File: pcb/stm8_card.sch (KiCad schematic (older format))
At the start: 22 parts, among them J1 DEBUG HEADER, SW1 TL59AF100Q, SW2 TL59AF100Q, SW3 TL59AF100Q, SW4 TL3302AF260QG, U1 ER-OLED0.91-7, U2 STM8S103F3

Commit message: pcb updated bat footprint in schematic not just board
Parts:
- BT1: footprint Battery:BatteryHolder_Keystone_103_1x20mm -> stm8_card:BatteryHolder_Keystone_103_1x20mm_Corrected
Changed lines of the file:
@@
 F 0 "BT1" H 1550 4500 50  0000 L CNN
 F 1 "103" H 1418 4405 50  0001 L CNN
-F 2 "Battery:BatteryHolder_Keystone_103_1x20mm" V 1300 4460 50  0001 C CNN
+F 2 "stm8_card:BatteryHolder_Keystone_103_1x20mm_Corrected" V 1300 4460 50  0001 C CNN
 F 3 "~" V 1300 4460 50  0001 C CNN
 F 4 "36-103-ND" H 1650 4400 50  0000 C CNN "digikey"

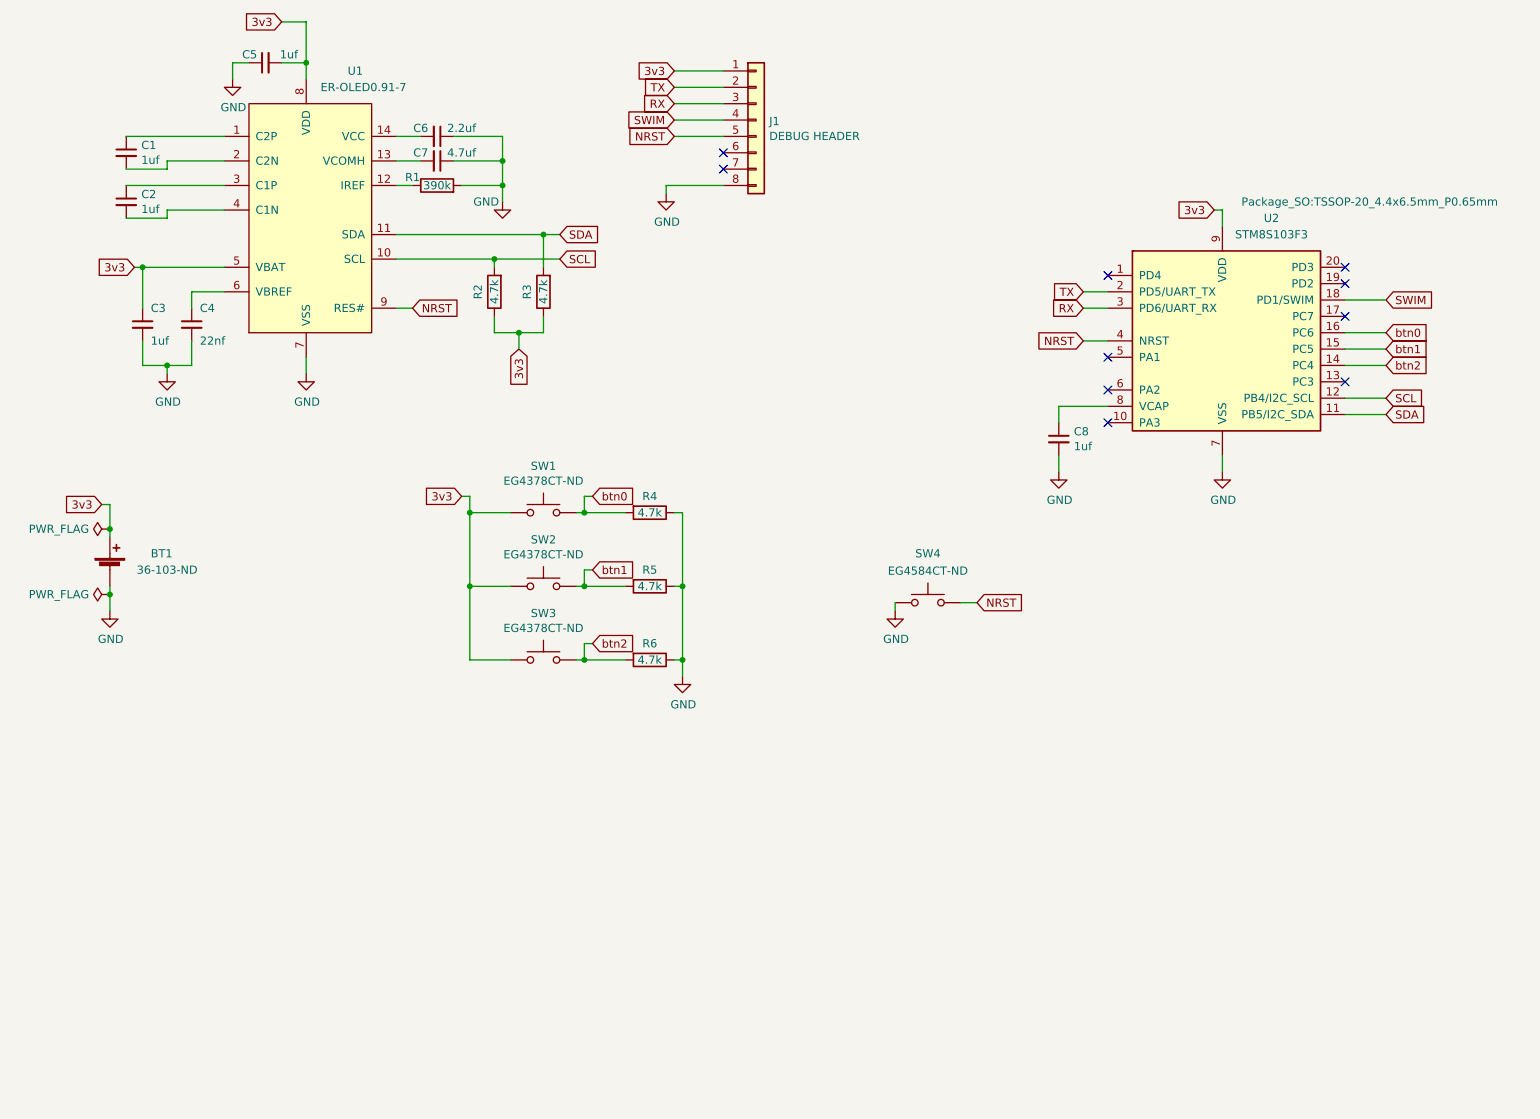
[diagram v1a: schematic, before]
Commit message: pcb improved pcb + added led, res, and mcu cap
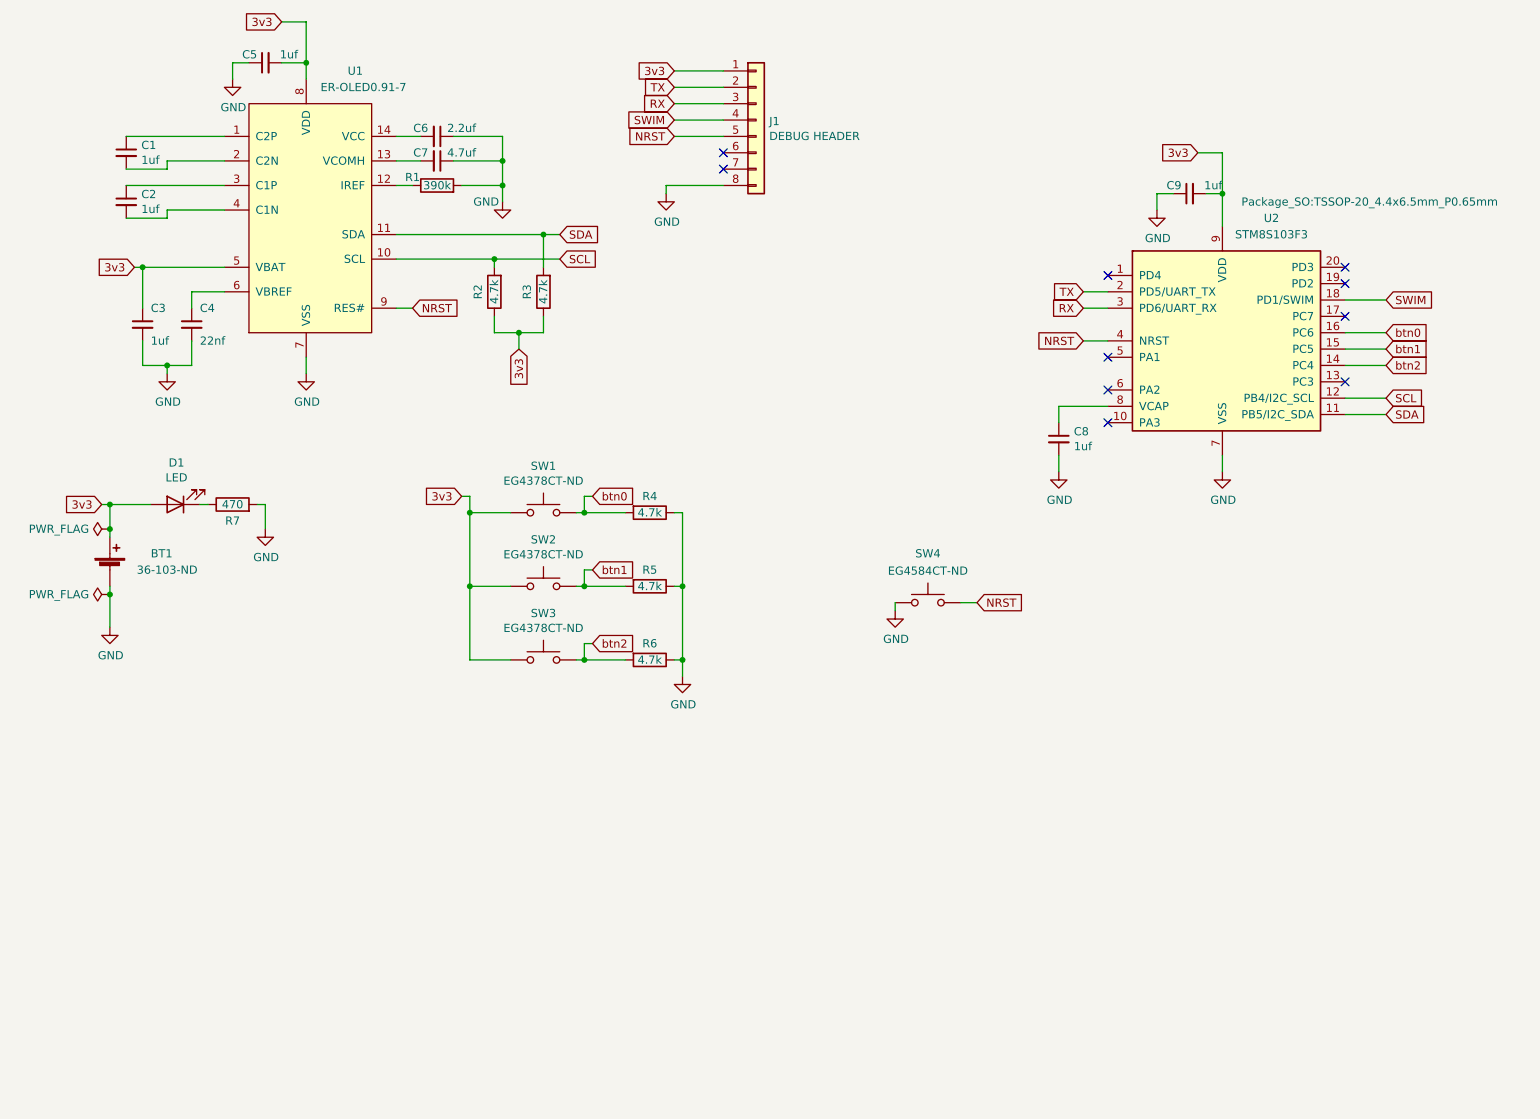
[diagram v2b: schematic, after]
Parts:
- added C9: 1uf, Capacitor_SMD:C_0805_2012Metric_Pad1.18x1.45mm_HandSolder, symbol Device:C_Small
- added D1: LED, stm8_card:LED_0805_2012Metric_Pad1.15x1.40mm_HandSolder, symbol Device:LED
- added R7: 470, Resistor_SMD:R_0805_2012Metric_Pad1.20x1.40mm_HandSolder, symbol Device:R
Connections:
- net 3v3: now also C9.2, D1.2 (A)
- net GND: now also C9.1, R7.2
- new net: D1.1 (K), R7.1
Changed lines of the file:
@@
 Wire Wire Line
 	8850 3450 9100 3450
-Text GLabel 8050 2200 0    50   Input ~ 0
+Text GLabel 7950 1850 0    50   Input ~ 0
 3v3
-Wire Wire Line
-	8050 2200 8100 2200
-Wire Wire Line
-	8100 2200 8100 2300
 Wire Wire Line
 	3150 2800 3050 2800
@@
 L power:GND #PWR01
 U 1 1 60827C7E
-P 1300 4650
-F 0 "#PWR01" H 1300 4400 50  0001 C CNN
-F 1 "GND" H 1305 4477 50  0000 C CNN
-F 2 "" H 1300 4650 50  0001 C CNN
-F 3 "" H 1300 4650 50  0001 C CNN
-	1    1300 4650
+P 2250 4150
+F 0 "#PWR01" H 2250 3900 50  0001 C CNN
+F 1 "GND" H 2255 3977 50  0000 C CNN
+F 2 "" H 2250 4150 50  0001 C CNN
+F 3 "" H 2250 4150 50  0001 C CNN
+	1    2250 4150
 	1    0    0    -1
 $EndComp
@@
 Connection ~ 1300 4550
 Wire Wire Line
-	1300 4550 1300 4650
-Wire Wire Line
 	2050 1300 2050 1400
 Wire Wire Line
@@
 Wire Wire Line
 	2350 1050 2500 1050
+$Comp
+L Device:C_Small C9
+U 1 1 6086F05B
+P 7900 2100
+F 0 "C9" V 7950 2150 50  0000 L CNN
+F 1 "1uf" V 7950 1900 50  0000 L CNN
+F 2 "Capacitor_SMD:C_0805_2012Metric_Pad1.18x1.45mm_HandSolder" H 7900 2100 50  0001 C CNN
+F 3 "~" H 7900 2100 50  0001 C CNN
+	1    7900 2100
+	0    -1   -1   0
+$EndComp
+$Comp
+L power:GND #PWR0101
+U 1 1 6086F703
+P 7700 2200
+F 0 "#PWR0101" H 7700 1950 50  0001 C CNN
+F 1 "GND" H 7705 2027 50  0000 C CNN
+F 2 "" H 7700 2200 50  0001 C CNN
+F 3 "" H 7700 2200 50  0001 C CNN
+	1    7700 2200
+	1    0    0    -1
+$EndComp
+Wire Wire Line
+	8100 1850 7950 1850
+Wire Wire Line
+	8100 1850 8100 2100
+Wire Wire Line
+	8000 2100 8100 2100
+Connection ~ 8100 2100
+Wire Wire Line
+	8100 2100 8100 2300
+Wire Wire Line
+	7800 2100 7700 2100
+Wire Wire Line
+	7700 2100 7700 2200
+$Comp
+L Device:R R7
+U 1 1 6087FF9F
+P 2050 4000
+F 0 "R7" V 1950 4000 50  0000 C CNN
+F 1 "470" V 2050 4000 50  0000 C CNN
+F 2 "Resistor_SMD:R_0805_2012Metric_Pad1.20x1.40mm_HandSolder" V 1980 4000 50  0001 C CNN
+F 3 "~" H 2050 4000 50  0001 C CNN
+	1    2050 4000
+	0    -1   -1   0
+$EndComp
+$Comp
+L Device:LED D1
+U 1 1 6088C1B4
+P 1700 4000
+F 0 "D1" H 1693 3745 50  0000 C CNN
+F 1 "LED" H 1693 3836 50  0000 C CNN
+F 2 "stm8_card:LED_0805_2012Metric_Pad1.15x1.40mm_HandSolder" H 1700 4000 50  0001 C CNN
+F 3 "~" H 1700 4000 50  0001 C CNN
+F 4 "404-1316-1-ND" H 1700 4000 50  0001 C CNN "digikey"
+	1    1700 4000
+	-1   0    0    1
+$EndComp
+Wire Wire Line
+	1300 4000 1550 4000
+Connection ~ 1300 4000
+Wire Wire Line
+	1850 4000 1900 4000
+Wire Wire Line
+	2250 4000 2250 4150
+Wire Wire Line
+	2200 4000 2250 4000
+$Comp
+L power:GND #PWR?
+U 1 1 608BFC4F
+P 1300 4750
+F 0 "#PWR?" H 1300 4500 50  0001 C CNN
+F 1 "GND" H 1305 4577 50  0000 C CNN
+F 2 "" H 1300 4750 50  0001 C CNN
+F 3 "" H 1300 4750 50  0001 C CNN
+	1    1300 4750
+	1    0    0    -1
+$EndComp
+Wire Wire Line
+	1300 4550 1300 4750
 $EndSCHEMATC

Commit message: rescued schematic library to newer version I think???
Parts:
- BT1: symbol Device:Battery_Cell -> stm8_card-rescue:Battery_Cell-Device
- C1, C2, C3, C4, C5, C6, C7, C8, C9: symbol Device:C_Small -> stm8_card-rescue:C_Small-Device
- D1: symbol Device:LED -> stm8_card-rescue:LED-Device
- J1: symbol Connector_Generic:Conn_01x08 -> stm8_card-rescue:Conn_01x08-Connector_Generic
- R1, R2, R3, R4, R5, R6, R7: symbol Device:R -> stm8_card-rescue:R-Device
- SW1, SW2, SW3, SW4: symbol Switch:SW_Push -> stm8_card-rescue:SW_Push-Switch
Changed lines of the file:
@@
 $EndComp
 $Comp
-L Switch:SW_Push SW1
+L stm8_card-rescue:SW_Push-Switch SW1
 U 1 1 608279B5
 P 3950 4050
@@
 $EndComp
 $Comp
-L Switch:SW_Push SW3
+L stm8_card-rescue:SW_Push-Switch SW3
 U 1 1 608281CA
 P 3950 4950
@@
 $EndComp
 $Comp
-L Switch:SW_Push SW2
+L stm8_card-rescue:SW_Push-Switch SW2
 U 1 1 608286D3
 P 3950 4500
@@
 $EndComp
 $Comp
-L Device:R R4
+L stm8_card-rescue:R-Device R4
 U 1 1 60813C31
 P 4600 4050
@@
 $EndComp
 $Comp
-L Device:R R5
+L stm8_card-rescue:R-Device R5
 U 1 1 608142DD
 P 4600 4500
@@
 $EndComp
 $Comp
-L Device:R R6
+L stm8_card-rescue:R-Device R6
 U 1 1 608145EE
 P 4600 4950
@@
 $EndComp
 $Comp
-L power:GND #PWR08
+L stm8_card-rescue:GND-power #PWR08
 U 1 1 6081C487
 P 6100 4650
@@
 $EndComp
 $Comp
-L Device:Battery_Cell BT1
+L stm8_card-rescue:Battery_Cell-Device BT1
 U 1 1 6081E543
 P 1300 4400
@@
 $EndComp
 $Comp
-L power:GND #PWR06
+L stm8_card-rescue:GND-power #PWR06
 U 1 1 6081EBFF
 P 4700 2100
@@
 	6100 4600 6100 4650
 $Comp
-L power:GND #PWR010
+L stm8_card-rescue:GND-power #PWR010
 U 1 1 6082B314
 P 8100 3800
@@
 $EndComp
 $Comp
-L Device:C_Small C1
+L stm8_card-rescue:C_Small-Device C1
 U 1 1 6082D715
 P 1400 1850
@@
 $EndComp
 $Comp
-L Device:C_Small C2
+L stm8_card-rescue:C_Small-Device C2
 U 1 1 6082E3CB
 P 1400 2150
@@
 	1650 2200 2000 2200
 $Comp
-L Switch:SW_Push SW4
+L stm8_card-rescue:SW_Push-Switch SW4
 U 1 1 60827F4F
 P 6300 4600
@@
 	4200 4850 4250 4850
 $Comp
-L power:GND #PWR04
+L stm8_card-rescue:GND-power #PWR04
 U 1 1 60844B9E
 P 2500 3200
@@
 	3650 2850 3650 2950
 $Comp
-L Device:R R3
+L stm8_card-rescue:R-Device R3
 U 1 1 60849F57
 P 3950 2700
@@
 $EndComp
 $Comp
-L Device:R R2
+L stm8_card-rescue:R-Device R2
 U 1 1 608498CA
 P 3650 2700
@@
 $EndComp
 $Comp
-L Device:R R1
+L stm8_card-rescue:R-Device R1
 U 1 1 608515E3
 P 3300 2050
@@
 $EndComp
 $Comp
-L Device:C_Small C7
+L stm8_card-rescue:C_Small-Device C7
 U 1 1 60851930
 P 3300 1900
@@
 $EndComp
 $Comp
-L Device:C_Small C6
+L stm8_card-rescue:C_Small-Device C6
 U 1 1 60851F1A
 P 3300 1750
@@
 $EndComp
 $Comp
-L power:GND #PWR05
+L stm8_card-rescue:GND-power #PWR05
 U 1 1 60852DD5
 P 3700 2150
@@
 	3700 2050 3700 2150
 $Comp
-L Device:C_Small C4
+L stm8_card-rescue:C_Small-Device C4
 U 1 1 6085DCB0
 P 1800 2900
@@
 $EndComp
 $Comp
-L power:GND #PWR02
+L stm8_card-rescue:GND-power #PWR02
 U 1 1 6085E004
 P 1650 3200
@@
 3v3
 $Comp
-L Device:C_Small C3
+L stm8_card-rescue:C_Small-Device C3
 U 1 1 608634F0
 P 1500 2900
@@
 	1800 2700 2000 2700
 $Comp
-L Connector_Generic:Conn_01x08 J1
+L stm8_card-rescue:Conn_01x08-Connector_Generic J1
 U 1 1 608162A6
 P 5250 1650
@@
 	7250 2800 7400 2800
 $Comp
-L Device:C_Small C8
+L stm8_card-rescue:C_Small-Device C8
 U 1 1 608B409C
 P 7100 3600
@@
 	7400 3400 7100 3400
 $Comp
-L power:GND #PWR09
+L stm8_card-rescue:GND-power #PWR09
 U 1 1 608B7854
 P 7100 3800
@@
 	8100 3800 8100 3700
 $Comp
-L power:GND #PWR07
+L stm8_card-rescue:GND-power #PWR07
 U 1 1 60813F2A
 P 4800 5050
@@
 	4800 4950 4800 5050
 $Comp
-L power:GND #PWR01
+L stm8_card-rescue:GND-power #PWR01
 U 1 1 60827C7E
 P 2250 4150
@@
 NoConn ~ 5050 1950
 $Comp
-L power:PWR_FLAG #FLG01
+L stm8_card-rescue:PWR_FLAG-power #FLG01
 U 1 1 6084AA5A
 P 1300 4150
@@
 $EndComp
 $Comp
-L power:PWR_FLAG #FLG02
+L stm8_card-rescue:PWR_FLAG-power #FLG02
 U 1 1 6084B498
 P 1300 4550
@@
 	2500 1300 2350 1300
 $Comp
-L power:GND #PWR03
+L stm8_card-rescue:GND-power #PWR03
 U 1 1 60888E69
 P 2050 1400
@@
 $EndComp
 $Comp
-L Device:C_Small C5
+L stm8_card-rescue:C_Small-Device C5
 U 1 1 608724BC
 P 2250 1300
@@
 	2350 1050 2500 1050
 $Comp
-L Device:C_Small C9
+L stm8_card-rescue:C_Small-Device C9
 U 1 1 6086F05B
 P 7900 2100
@@
 $EndComp
 $Comp
-L power:GND #PWR0101
+L stm8_card-rescue:GND-power #PWR0101
 U 1 1 6086F703
 P 7700 2200
@@
 	7700 2100 7700 2200
 $Comp
-L Device:R R7
+L stm8_card-rescue:R-Device R7
 U 1 1 6087FF9F
 P 2050 4000
@@
 $EndComp
 $Comp
-L Device:LED D1
+L stm8_card-rescue:LED-Device D1
 U 1 1 6088C1B4
 P 1700 4000
@@
 	2200 4000 2250 4000
 $Comp
-L power:GND #PWR?
+L stm8_card-rescue:GND-power #PWR?
 U 1 1 608BFC4F
 P 1300 4750

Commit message: rough schematic update
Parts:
- removed BT1: 103, stm8_card:BatteryHolder_Keystone_103_1x20mm_Corrected, symbol stm8_card-rescue:Battery_Cell-Device
- added C10: 330mF, symbol Device:C
- added C? (x2): 1uf, Capacitor_SMD:C_0805_2012Metric_Pad1.18x1.45mm_HandSolder, symbol stm8_card-rescue:C_Small-Device
- added C?: 0.1uF, Capacitor_SMD:C_0805_2012Metric_Pad1.18x1.45mm_HandSolder, symbol stm8_card-rescue:C_Small-Device
- added J?: USB_C_Receptacle_USB2.0, symbol Connector:USB_C_Receptacle_USB2.0
- added R?: 470, Resistor_SMD:R_0805_2012Metric_Pad1.20x1.40mm_HandSolder, symbol stm8_card-rescue:R-Device
- added U?: MIC5253-3.3YC5, Package_TO_SOT_SMD:SOT-23-5, symbol Regulator_Linear:MIC5205-3.3YM5
- R7: value 470 -> 4.7k
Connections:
- net 3v3: now also C10.1, R?.2
- net GND: now also C10.2, C?.2, C?.2, C?.2, J?.A1 (GND), J?.A12 (GND), J?.B1 (GND), J?.B12 (GND), U?.2 (GND)
- new net: C?.1, J?.A4 (VBUS), J?.A9 (VBUS), J?.B4 (VBUS), J?.B9 (VBUS), U?.1 (IN), U?.3 (EN)
- new net: C?.1, U?.4 (BP)
- new net: C?.1, R?.1, U?.5 (OUT)
- no-connect marks 10 -> 19
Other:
- moved on the sheet: D1, R7
